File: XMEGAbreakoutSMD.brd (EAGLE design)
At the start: 160 x 100 mm, 22 parts, among them IC1 XMEGA16A4

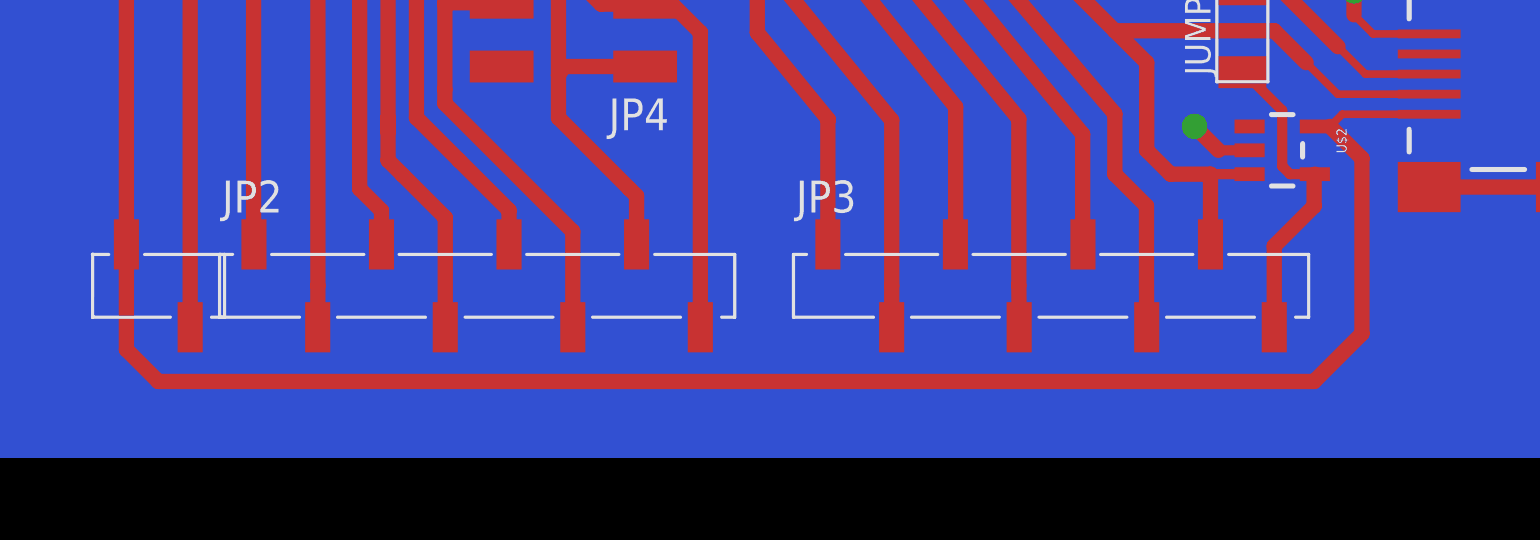
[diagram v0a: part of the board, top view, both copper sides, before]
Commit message: solder jumper on 5V
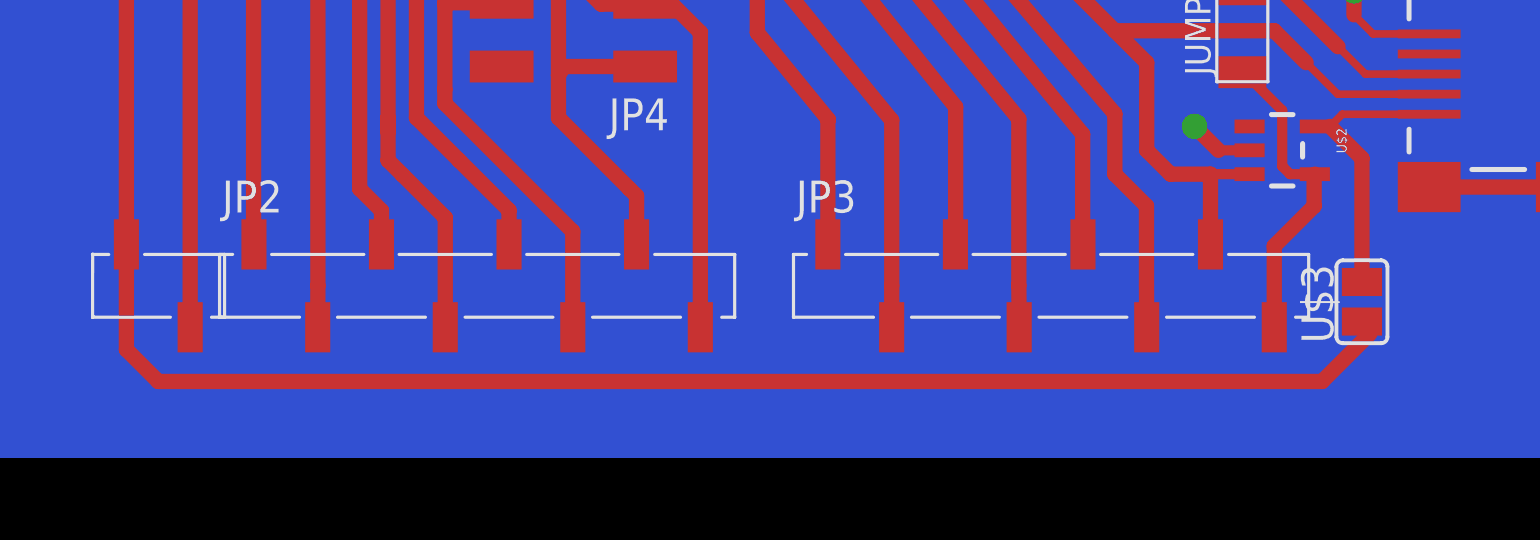
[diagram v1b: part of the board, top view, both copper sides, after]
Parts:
- added U$3: SOLDER_JUMPER, fab:SJFAB
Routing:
- net VBUS: track 104.7 -> 102.8 mm
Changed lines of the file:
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@@
 <layer number="17" name="Pads" color="2" fill="1" visible="yes" active="yes"/>
 <layer number="18" name="Vias" color="2" fill="1" visible="yes" active="yes"/>
-<layer number="19" name="Unrouted" color="6" fill="1" visible="yes" active="yes"/>
+<layer number="19" name="Unrouted" color="6" fill="1" visible="no" active="yes"/>
 <layer number="20" name="Dimension" color="15" fill="1" visible="no" active="yes"/>
 <layer number="21" name="tPlace" color="7" fill="1" visible="no" active="yes"/>
@@
 <element name="JP6" library="fab" package="2X03SMD" value="" x="84.582" y="60.071" rot="R180"/>
 <element name="JUMPER" library="fab" package="R1206FAB" value="0Ohm" x="88.9" y="31.75" rot="R90"/>
+<element name="U$3" library="fab" package="SJFAB" value="SOLDER_JUMPER" x="93.6625" y="20.955" rot="R90"/>
 </elements>
 <signals>
@@
 <contactref element="U$2" pad="5"/>
 <contactref element="JP9" pad="2"/>
-<wire x1="91.7575" y1="17.78" x2="45.72" y2="17.78" width="0.6096" layer="1"/>
+<wire x1="92.075" y1="17.78" x2="45.72" y2="17.78" width="0.6096" layer="1"/>
 <wire x1="43.7103375" y1="36.495978125" x2="44.115978125" y2="36.495978125" width="0.6096" layer="1"/>
 <wire x1="44.115978125" y1="36.495978125" x2="45.72" y2="38.1" width="0.6096" layer="1"/>
@@
 <wire x1="92.3925" y1="27.94" x2="91.7901" y2="27.94" width="0.3048" layer="1"/>
 <wire x1="91.7901" y1="27.94" x2="91.7876" y2="27.9375" width="0.3048" layer="1"/>
-<wire x1="91.7575" y1="17.78" x2="93.6625" y2="19.685" width="0.6096" layer="1"/>
-<wire x1="93.6625" y1="19.685" x2="93.6625" y2="26.67" width="0.6096" layer="1"/>
 <wire x1="93.6625" y1="26.67" x2="92.3925" y2="27.94" width="0.6096" layer="1"/>
+<wire x1="92.075" y1="17.78" x2="93.98" y2="19.685" width="0.6096" layer="1"/>
+<wire x1="93.6625" y1="26.67" x2="93.6625" y2="21.9075" width="0.6096" layer="1"/>
+<wire x1="93.98" y1="19.685" x2="93.6625" y2="21.9075" width="0" layer="19" extent="1-1"/>
 </signal>
 <signal name="D+">
@@
 <wire x1="90.4875" y1="26.3525" x2="90.4875" y2="28.575" width="0.4064" layer="1"/>
 <wire x1="90.4875" y1="28.575" x2="88.9" y2="30.1625" width="0.4064" layer="1"/>
-<wire x1="88.9" y1="30.1625" x2="88.9" y2="33.3375" width="0" layer="19" extent="1-16"/>
+<wire x1="90.4875" y1="28.575" x2="92.71" y2="31.115" width="0" layer="19" extent="1-1"/>
 </signal>
 <signal name="GND">
@@
 <wire x1="95.92080625" y1="37.81830625" x2="93.345" y2="35.2425" width="0.6096" layer="1"/>
 <wire x1="93.345" y1="35.2425" x2="93.345" y2="33.3375" width="0.6096" layer="1"/>
+<wire x1="87.9475" y1="26.9875" x2="89.1874" y2="26.9875" width="0.4064" layer="1"/>
 <wire x1="43.815" y1="52.2039375" x2="43.46418125" y2="50.095684375" width="0" layer="19" extent="1-16"/>
-<wire x1="87.9475" y1="26.9875" x2="89.1874" y2="26.9875" width="0.4064" layer="1"/>
 </signal>
 <signal name="VCC">

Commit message: smd
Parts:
- added C3: 0.1uF, fab:C1206FAB
- added C6, C7: 0.1uF, fab:C1206
- moved C2 49.7 mm to (11.6, 30.1), turned to 270 degrees
- moved JP6 45.8 mm to (42.3, 42.7)
- moved C4 45.5 mm to (59.8, 24.1)
- moved C5 45.5 mm to (5.08, 36.8)
- moved IC2 45.5 mm to (4.70, 32.3)
- moved JP4 45.5 mm to (20.3, 15.1)
- moved JUMPER 45.5 mm to (47.0, 14.0)
- moved LED1 45.5 mm to (1.71, 25.5)
- moved R1 45.5 mm to (41.6, 31.6)
- moved R2 45.5 mm to (1.80, 20.4)
- moved S1 45.5 mm to (46.3, 31.9)
- moved IC1 45.5 mm to (31.9, 26.7)
- moved JP1 45.5 mm to (58.5, 44.5)
- moved JP5 45.5 mm to (7.62, 44.5)
- moved JP8 45.5 mm to (2.54, 44.5)
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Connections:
- net GND: now also C3.2, C6.2, C7.2
- net VCC: now also C3.1, C6.1, C7.1
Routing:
- net GND: track 228.3 -> 261.4 mm, vias 9 -> 14
- net VCC: track 77.2 -> 90.5 mm
- net PE3: track 37.6 -> 34.7 mm
- net PE2: track 36.9 -> 34.4 mm
- net VBUS: track 102.8 -> 100.4 mm
- net N$13: track 34.6 -> 32.8 mm
- net N$23: track 20.6 -> 18.8 mm
- net N$9: track 30.9 -> 29.2 mm
- net PE0: track 43.7 -> 45.3 mm
- net PE1: track 43.6 -> 45.1 mm
- net N$16: track 37.9 -> 36.6 mm
- net MISO: track 28.0 -> 26.7 mm
- net SCK: track 28.7 -> 27.4 mm
- net N$12: track 30.2 -> 29.0 mm
- net N$14: track 31.3 -> 30.1 mm
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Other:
- board size 160 x 100 mm -> 62.2 x 48.3 mm
